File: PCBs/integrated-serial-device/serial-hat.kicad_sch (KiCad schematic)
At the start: 20 parts, among them CN1 Modem port, CN2 Modem out 3, CN3 Printer port, J1 Rpi headers, K1 Quicktake, K2 ImageWriter, SW1 Modem To Proxy, SW2 Modem to Quicktake, SW3 Modem out 3, SW4 Printer out 3, SW5 Printer to Proxy, SW6 Printer to ImageWriter, U1 MAX3232

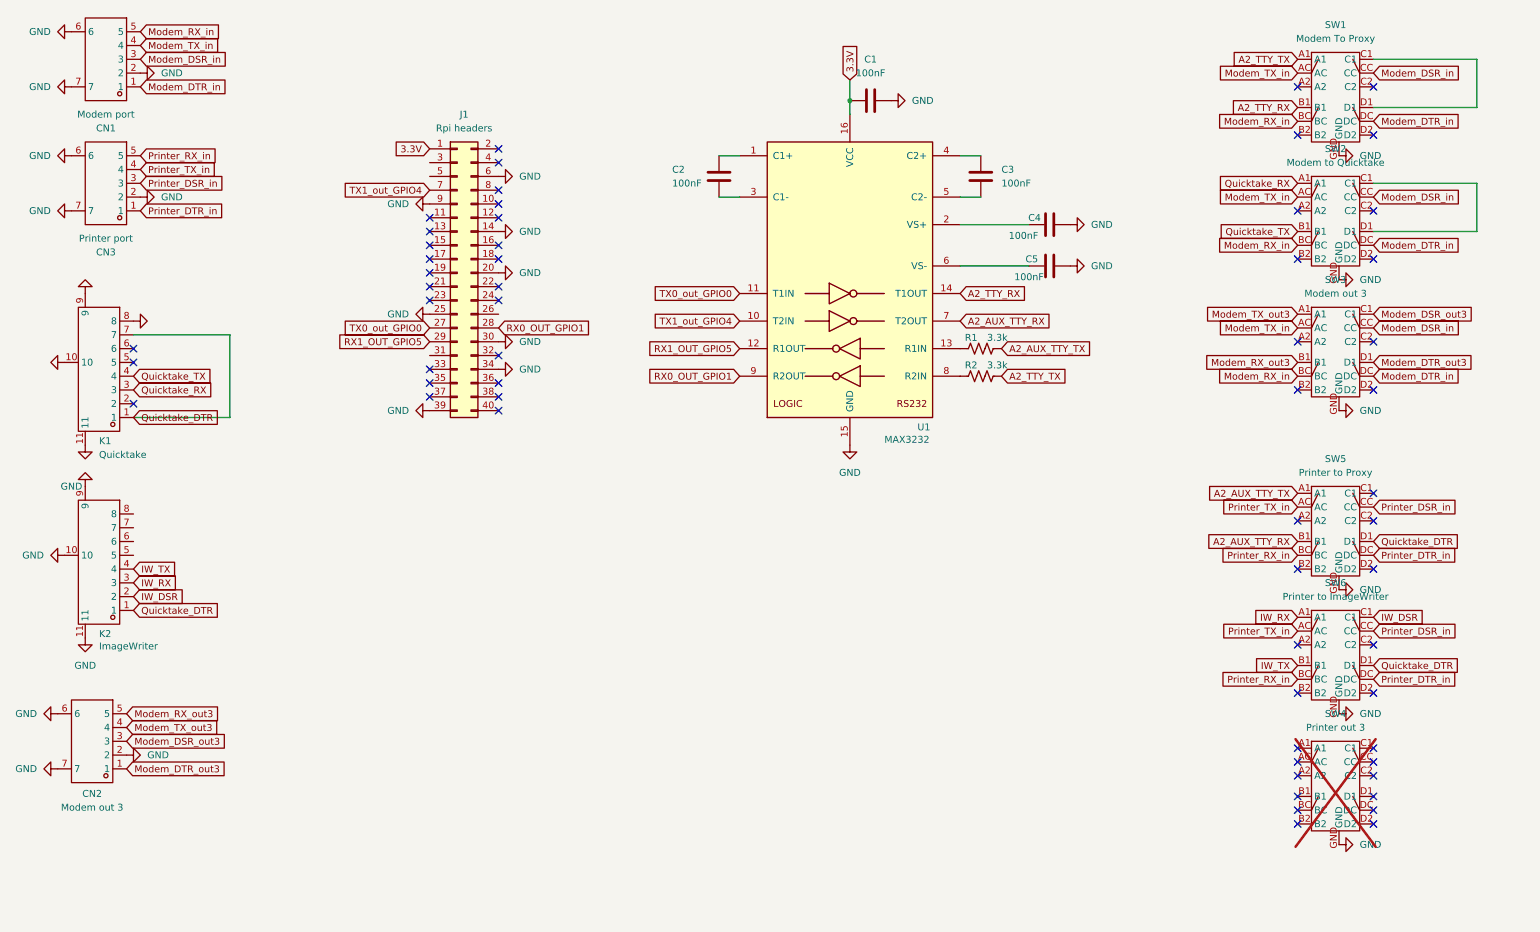
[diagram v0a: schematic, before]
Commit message: Add jumper for IIc/IIgs
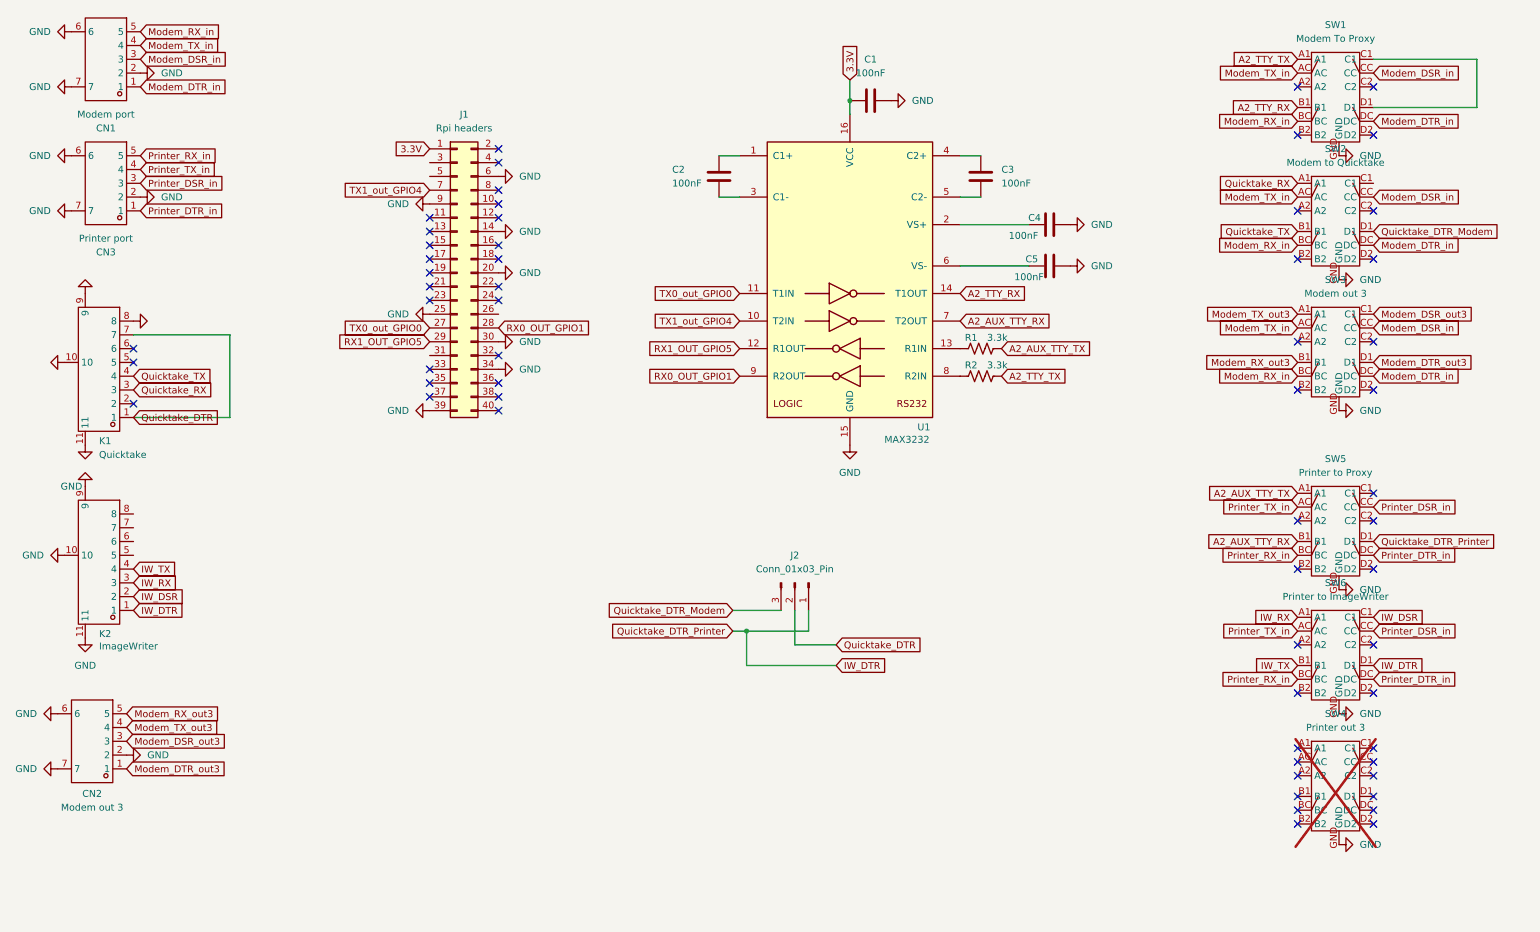
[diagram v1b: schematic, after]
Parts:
- added J2: Conn_01x03_Pin, Connector_PinHeader_2.54mm:PinHeader_1x03_P2.54mm_Vertical, symbol Connector:Conn_01x03_Pin
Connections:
- net Quicktake_DTR: now also J2.2 (Pin_2); no longer K2.1, SW5.D1, SW6.D1
- net at SW2.C1: no longer SW2.D1
- new net IW_DTR: J2.1 (Pin_1), K2.1, SW5.D1, SW6.D1
- new net Quicktake_DTR_Modem: J2.3 (Pin_3), SW2.D1
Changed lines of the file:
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@@
 		(color 0 0 0 0)
 	)
+	(junction
+		(at 146.05 127)
+		(diameter 0)
+		(color 0 0 0 0)
+	)
 	(no_connect
 		(at 247.65 49.53)
@@
 	(wire
 		(pts
+			(xy 157.48 127) (xy 146.05 127)
+		)
+		(stroke
+			(width 0)
+			(type default)
+		)
+	)
+	(wire
+		(pts
+			(xy 146.05 127) (xy 143.51 127)
+		)
+		(stroke
+			(width 0)
+			(type default)
+		)
+	)
+	(wire
+		(pts
 			(xy 165.1 29.21) (xy 165.1 31.75)
 		)
@@
 	(wire
 		(pts
+			(xy 143.51 123.19) (xy 152.4 123.19)
+		)
+		(stroke
+			(width 0)
+			(type default)
+		)
+	)
+	(wire
+		(pts
+			(xy 154.94 123.19) (xy 154.94 129.54)
+		)
+		(stroke
+			(width 0)
+			(type default)
+		)
+	)
+	(wire
+		(pts
 			(xy 165.1 25.4) (xy 165.1 29.21)
 		)
@@
 	(wire
 		(pts
+			(xy 154.94 129.54) (xy 162.56 129.54)
+		)
+		(stroke
+			(width 0)
+			(type default)
+		)
+	)
+	(wire
+		(pts
 			(xy 185.42 59.69) (xy 198.12 59.69)
 		)
@@
 	(wire
 		(pts
-			(xy 261.62 53.34) (xy 280.67 53.34)
+			(xy 140.97 39.37) (xy 144.78 39.37)
 		)
 		(stroke
@@
 	(wire
 		(pts
-			(xy 140.97 39.37) (xy 144.78 39.37)
+			(xy 146.05 133.35) (xy 162.56 133.35)
 		)
 		(stroke
@@
 	(wire
 		(pts
-			(xy 280.67 21.59) (xy 280.67 30.48)
+			(xy 146.05 127) (xy 146.05 133.35)
 		)
 		(stroke
@@
 	(wire
 		(pts
-			(xy 280.67 44.45) (xy 280.67 53.34)
+			(xy 280.67 21.59) (xy 280.67 30.48)
 		)
 		(stroke
@@
 	(wire
 		(pts
-			(xy 50.8 87.63) (xy 50.8 72.39)
+			(xy 157.48 123.19) (xy 157.48 127)
 		)
 		(stroke
@@
 	(wire
 		(pts
-			(xy 140.97 46.99) (xy 144.78 46.99)
+			(xy 50.8 87.63) (xy 50.8 72.39)
 		)
 		(stroke
@@
 	(wire
 		(pts
-			(xy 261.62 44.45) (xy 280.67 44.45)
+			(xy 140.97 46.99) (xy 144.78 46.99)
 		)
 		(stroke
@@
 		)
 	)
+	(global_label "Quicktake_DTR_Printer"
+		(shape input)
+		(at 143.51 127 180)
+		(fields_autoplaced yes)
+		(effects
+			(font
+				(size 1.27 1.27)
+			)
+			(justify right)
+		)
+		(property "Intersheetrefs" "${INTERSHEET_REFS}"
+			(at 119.4791 127 0)
+			(effects
+				(font
+					(size 1.27 1.27)
+				)
+				(justify right)
+				(hide yes)
+			)
+		)
+	)
 	(global_label "Modem_TX_in"
 		(shape input)
@@
 		)
 	)
+	(global_label "Quicktake_DTR_Modem"
+		(shape input)
+		(at 261.62 53.34 0)
+		(fields_autoplaced yes)
+		(effects
+			(font
+				(size 1.27 1.27)
+			)
+			(justify left)
+		)
+		(property "Intersheetrefs" "${INTERSHEET_REFS}"
+			(at 285.7717 53.34 0)
+			(effects
+				(font
+					(size 1.27 1.27)
+				)
+				(justify left)
+				(hide yes)
+			)
+		)
+	)
 	(global_label "A2_AUX_TTY_RX"
 		(shape input)
@@
 		)
 	)
+	(global_label "Quicktake_DTR_Printer"
+		(shape input)
+		(at 261.62 110.49 0)
+		(fields_autoplaced yes)
+		(effects
+			(font
+				(size 1.27 1.27)
+			)
+			(justify left)
+		)
+		(property "Intersheetrefs" "${INTERSHEET_REFS}"
+			(at 285.6509 110.49 0)
+			(effects
+				(font
+					(size 1.27 1.27)
+				)
+				(justify left)
+				(hide yes)
+			)
+		)
+	)
+	(global_label "IW_DTR"
+		(shape input)
+		(at 162.56 133.35 0)
+		(fields_autoplaced yes)
+		(effects
+			(font
+				(size 1.27 1.27)
+			)
+			(justify left)
+		)
+		(property "Intersheetrefs" "${INTERSHEET_REFS}"
+			(at 172.0766 133.35 0)
+			(effects
+				(font
+					(size 1.27 1.27)
+				)
+				(justify left)
+				(hide yes)
+			)
+		)
+	)
 	(global_label "A2_AUX_TTY_TX"
 		(shape input)
@@
 		)
 	)
+	(global_label "IW_DTR"
+		(shape input)
+		(at 33.02 123.19 0)
+		(fields_autoplaced yes)
+		(effects
+			(font
+				(size 1.27 1.27)
+			)
+			(justify left)
+		)
+		(property "Intersheetrefs" "${INTERSHEET_REFS}"
+			(at 42.5366 123.19 0)
+			(effects
+				(font
+					(size 1.27 1.27)
+				)
+				(justify left)
+				(hide yes)
+			)
+		)
+	)
 	(global_label "Printer_DSR_in"
 		(shape input)
@@
 		)
 	)
+	(global_label "Quicktake_DTR"
+		(shape input)
+		(at 162.56 129.54 0)
+		(fields_autoplaced yes)
+		(effects
+			(font
+				(size 1.27 1.27)
+			)
+			(justify left)
+		)
+		(property "Intersheetrefs" "${INTERSHEET_REFS}"
+			(at 179.2128 129.54 0)
+			(effects
+				(font
+					(size 1.27 1.27)
+				)
+				(justify left)
+				(hide yes)
+			)
+		)
+	)
 	(global_label "A2_TTY_RX"
 		(shape input)
@@
 		)
 	)
-	(global_label "Quicktake_DTR"
-		(shape input)
-		(at 33.02 123.19 0)
-		(fields_autoplaced yes)
-		(effects
-			(font
-				(size 1.27 1.27)
-			)
-			(justify left)
-		)
-		(property "Intersheetrefs" "${INTERSHEET_REFS}"
-			(at 49.6728 123.19 0)
-			(effects
-				(font
-					(size 1.27 1.27)
-				)
-				(justify left)
-				(hide yes)
-			)
-		)
-	)
 	(global_label "Modem_DSR_out3"
 		(shape input)
@@
 		)
 	)
-	(global_label "Quicktake_DTR"
+	(global_label "Modem_RX_out3"
 		(shape input)
-		(at 261.62 133.35 0)
+		(at 31.75 142.24 0)
 		(fields_autoplaced yes)
 		(effects
@@
 		)
 		(property "Intersheetrefs" "${INTERSHEET_REFS}"
-			(at 278.2728 133.35 0)
+			(at 49.9144 142.24 0)
 			(effects
 				(font
@@
 		)
 	)
-	(global_label "Modem_RX_out3"
+	(global_label "Modem_DTR_in"
 		(shape input)
-		(at 31.75 142.24 0)
+		(at 261.62 33.02 0)
 		(fields_autoplaced yes)
 		(effects
@@
 		)
 		(property "Intersheetrefs" "${INTERSHEET_REFS}"
-			(at 49.9144 142.24 0)
+			(at 278.3331 33.02 0)
 			(effects
 				(font
@@
 		)
 	)
-	(global_label "Modem_DTR_in"
+	(global_label "IW_DTR"
 		(shape input)
-		(at 261.62 33.02 0)
+		(at 261.62 133.35 0)
 		(fields_autoplaced yes)
 		(effects
@@
 		)
 		(property "Intersheetrefs" "${INTERSHEET_REFS}"
-			(at 278.3331 33.02 0)
+			(at 271.1366 133.35 0)
 			(effects
 				(font
@@
 		)
 	)
-	(global_label "Quicktake_DTR"
+	(global_label "Quicktake_DTR_Modem"
 		(shape input)
-		(at 261.62 110.49 0)
+		(at 143.51 123.19 180)
 		(fields_autoplaced yes)
 		(effects
@@
 				(size 1.27 1.27)
 			)
-			(justify left)
+			(justify right)
 		)
 		(property "Intersheetrefs" "${INTERSHEET_REFS}"
-			(at 278.2728 110.49 0)
+			(at 119.3583 123.19 0)
 			(effects
 				(font
 					(size 1.27 1.27)
 				)
-				(justify left)
+				(justify right)
 				(hide yes)
 			)
@@
 					(unit 1)
 				)
+			)
+		)
+	)
+	(symbol
+		(lib_id "Connector:Conn_01x03_Pin")
+		(at 154.94 118.11 270)
+		(unit 1)
+		(exclude_from_sim no)
+		(in_bom yes)
+		(on_board yes)
+		(dnp no)
+		(fields_autoplaced yes)
+		(property "Reference" "J2"
+			(at 154.94 113.03 90)
+			(effects
+				(font
+					(size 1.27 1.27)
+				)
+			)
+		)
+		(property "Value" "Conn_01x03_Pin"
+			(at 154.94 115.57 90)
+			(effects
+				(font
+					(size 1.27 1.27)
+				)
+			)
+		)
+		(property "Footprint" "Connector_PinHeader_2.54mm:PinHeader_1x03_P2.54mm_Vertical"
+			(at 154.94 118.11 0)
+			(effects
+				(font
+					(size 1.27 1.27)
+				)
+				(hide yes)
+			)
+		)
+		(property "Datasheet" "~"
+			(at 154.94 118.11 0)
+			(effects
+				(font
+					(size 1.27 1.27)
+				)
+				(hide yes)
+			)
+		)
+		(property "Description" "Generic connector, single row, 01x03, script generated"
+			(at 154.94 118.11 0)
+			(effects
+				(font
+					(size 1.27 1.27)
+				)
+				(hide yes)
+			)
+		)
+		(pin "1"
+		)
+		(pin "2"
+		)
+		(pin "3"
+		)
+		(instances
+			(project "serial-hat"
+				(path "/f30a5902-bf77-48c6-ab50-b8e2235ec207"
+					(reference "J2")
+					(unit 1)
+				)

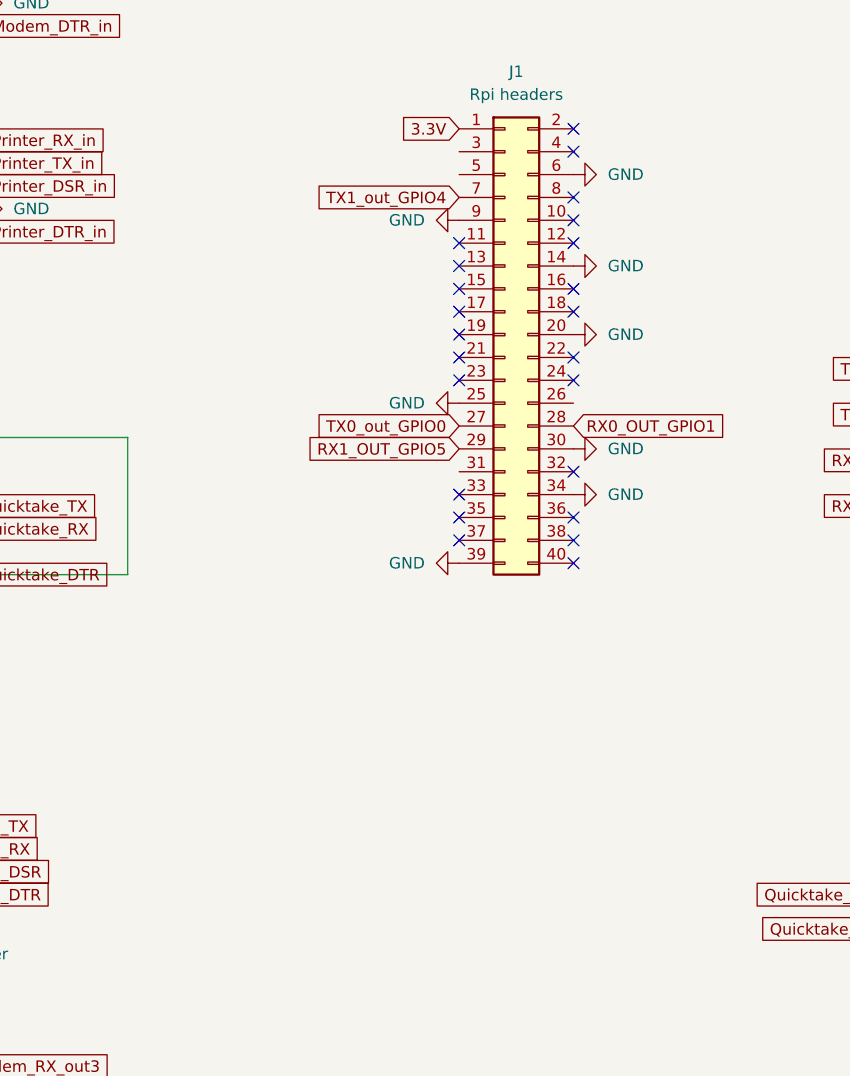
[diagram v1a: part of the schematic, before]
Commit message: Add enclosures
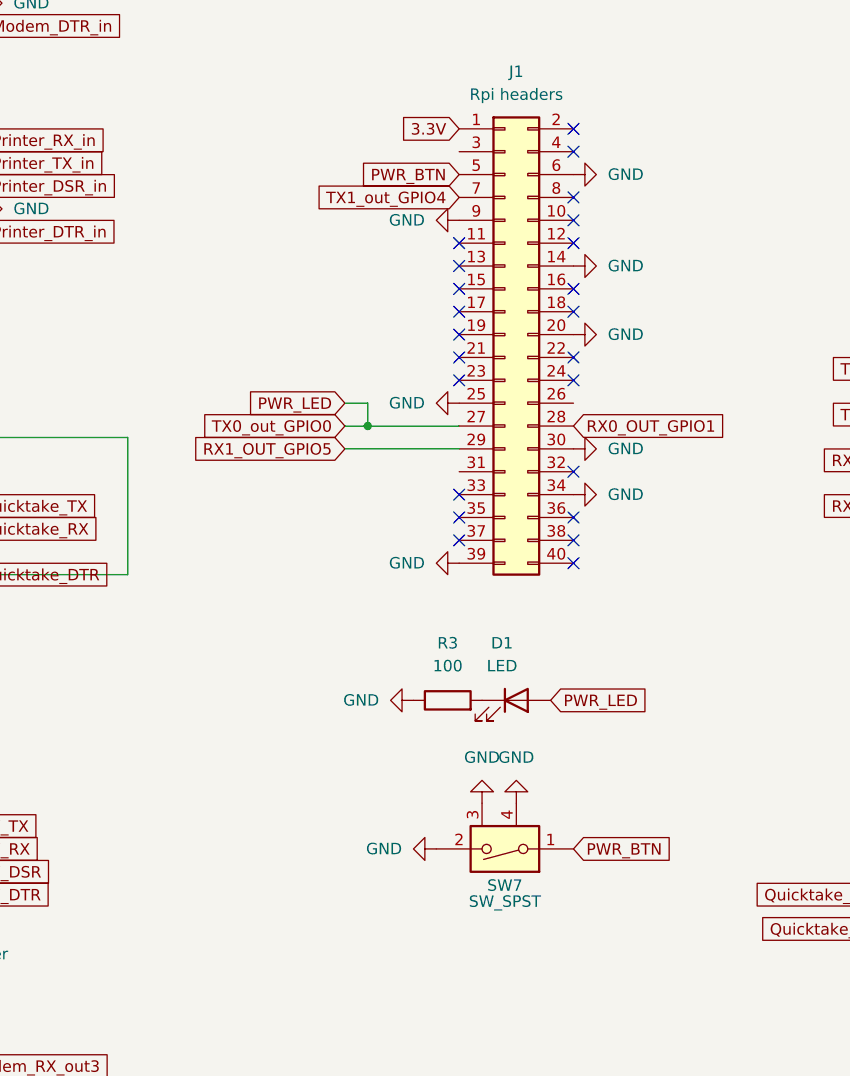
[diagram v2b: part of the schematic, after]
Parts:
- added D1: LED, LED_SMD:LED_0603_1608Metric, symbol Device:LED
- added R3: 100, Resistor_SMD:R_0603_1608Metric, symbol Device:R
- added SW7: SW_SPST, DIN5:SPST_power_switch, symbol Switch:SW_DIP_x01
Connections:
- net GND: now also R3.1, SW7.2, SW7.3, SW7.4 (3)
- net PWR_BTN: now reaches J1.5 (Pin_5)
- net PWR_BTN: now also SW7.1
- net TX0_out_GPIO0 renamed PWR_LED
- net PWR_LED: now also D1.2 (A)
- new net: D1.1 (K), R3.2
